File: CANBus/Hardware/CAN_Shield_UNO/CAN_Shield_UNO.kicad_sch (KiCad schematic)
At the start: 12 parts, among them J1 Power, J2 Digital/PWM, J3 Analog, J4 Digital/PWM, J7 Screw_Terminal_01x02, U2 TCAN1051HGV

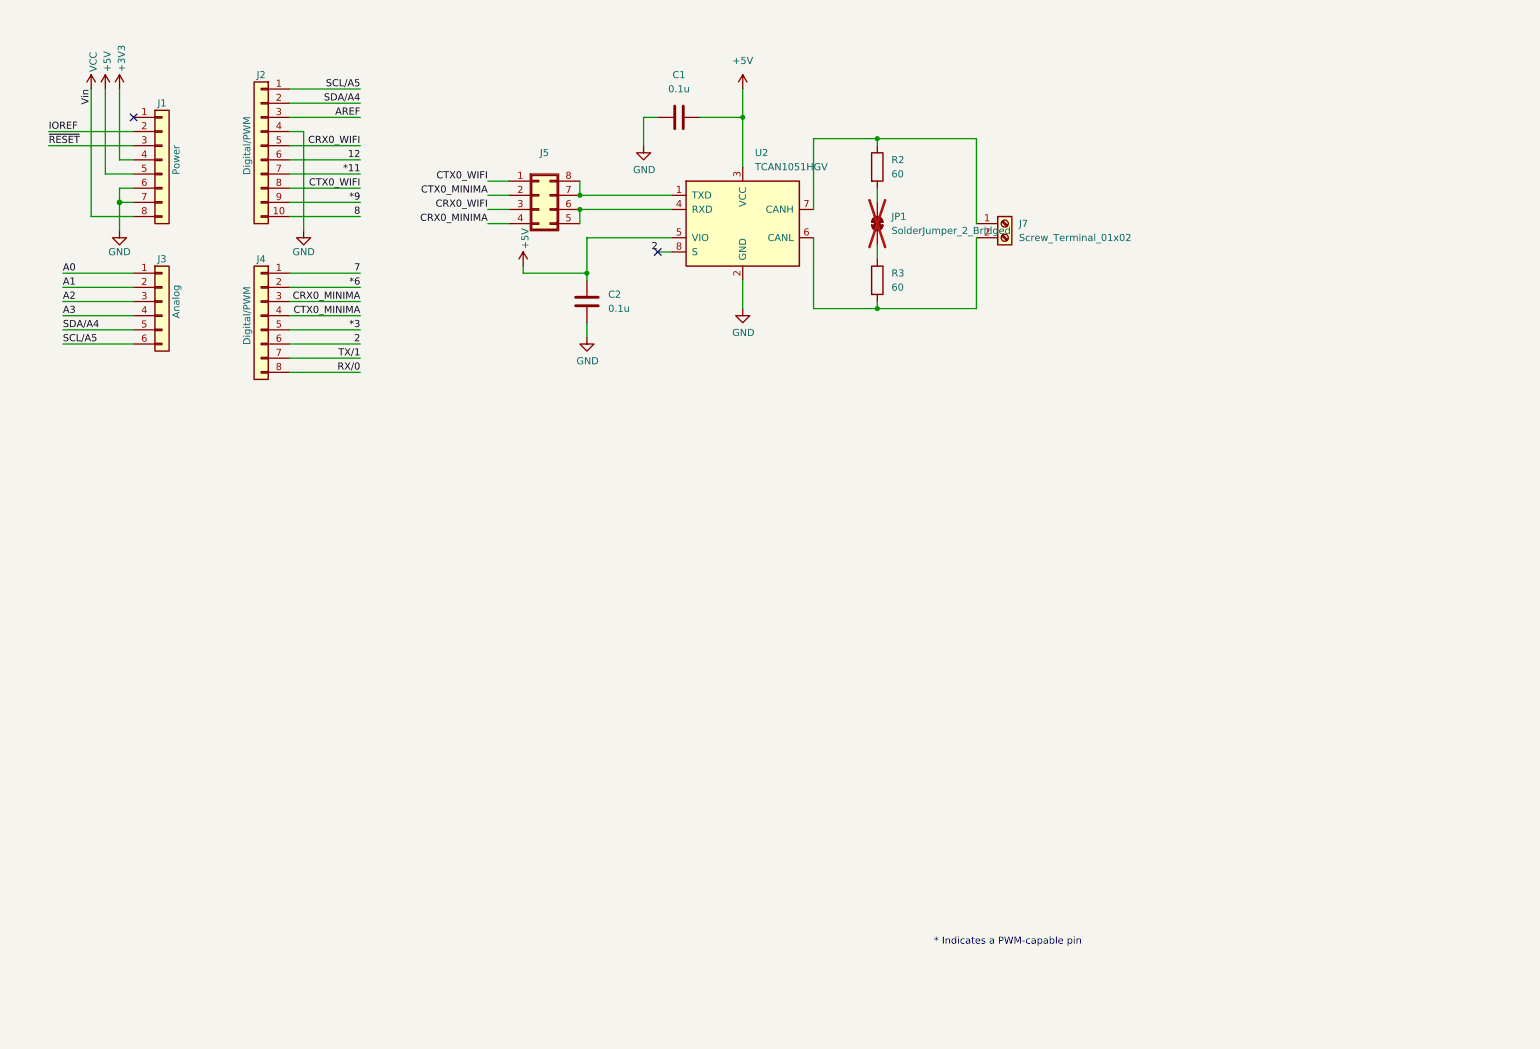
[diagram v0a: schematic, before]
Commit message: feat(hw): to add hardware components
- Replacing the CAN Bus driver
- Adding a pull-down resistor to the CS pin
- Adding a 1nF capacitor to the 120 ohm terminating resistor
- Adding 2EDN7534F (54 Gate driver) channels to handle high current outputs; in addition adding a diode to power them if the board is only powered through USB
- Adding TL4050A50IDBZT (Precision micropower shunt voltage) to generate a precise 5V reference
- Adding protection diodes for A0 and A1 analog inputs
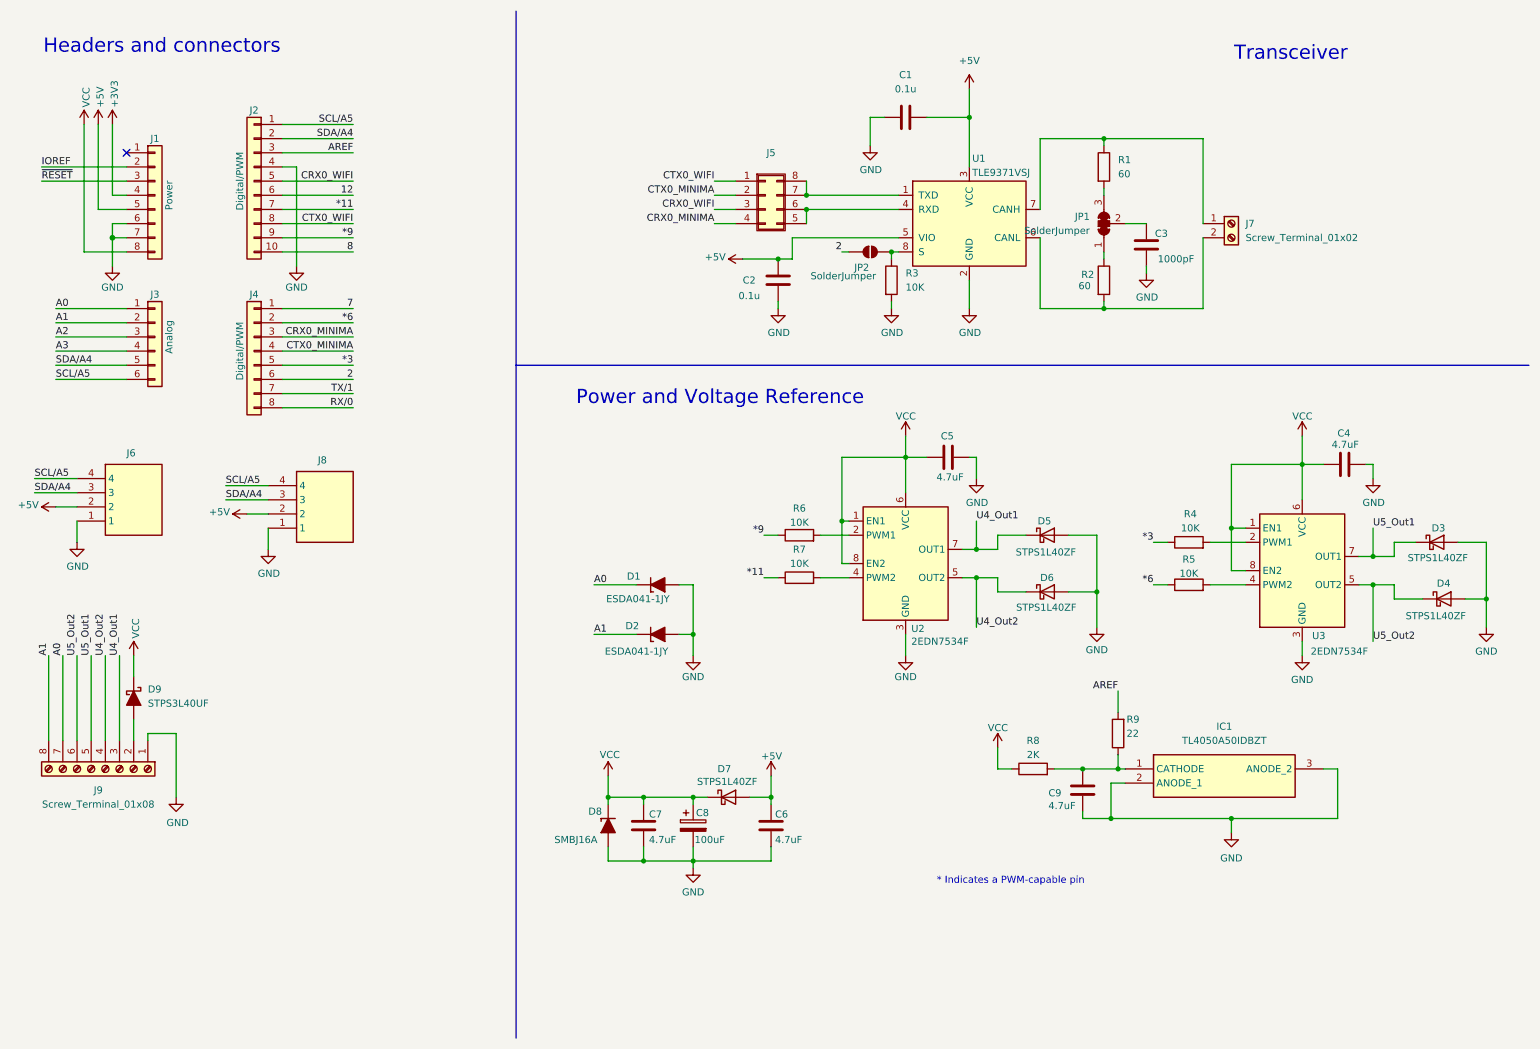
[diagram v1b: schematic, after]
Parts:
- removed JP1: SolderJumper_2_Bridged, Jumper:SolderJumper-2_P1.3mm_Bridged_Pad1.0x1.5mm, symbol Jumper:SolderJumper_2_Bridged
- added C3: 1000pF, Capacitor_SMD:C_0805_2012Metric_Pad1.18x1.45mm_HandSolder, symbol Device:C
- added C4, C5, C6, C7, C9: 4.7uF, Capacitor_SMD:C_1210_3225Metric_Pad1.33x2.70mm_HandSolder, symbol Device:C
- added C8: 100uF, Capacitor_SMD:CP_Elec_6.3x7.7, symbol PCM_Capacitor_AKL:CP_SMD_D6.3mm_H7.7mm
- added D1, D2: ESDA041-1JY, PCM_Diode_SMD_AKL:D_SOD-323, symbol PCM_Diode_TVS_AKL:SD05
- added D3, D4, D5, D6, D7: STPS1L40ZF, Diode_SMD:D_SOD-123, symbol Diode:MBR0540
- added D8: SMBJ16A, Diode_SMD:D_SMB, symbol PCM_Diode_TVS_AKL:SMBJ16A
- added D9: STPS3L40UF, Diode_SMD:D_SMB, symbol PCM_Diode_Schottky_AKL:STPS3L40UF
- added IC1: TL4050A50IDBZT, Package_TO_SOT_SMD:SOT-23-3, symbol TL4050A50IDBZT:TL4050A50IDBZT
- added J6, J8: Grove connector, Connector_PinHeader_2.54mm:PinHeader_1x04_P2.54mm_Vertical, symbol 110990030:110990030
- added J9: Screw_Terminal_01x08, TerminalBlock:TerminalBlock_bornier-8_P5.08mm, symbol Connector:Screw_Terminal_01x08
- added JP1: SolderJumper, Jumper:SolderJumper-3_P1.3mm_Open_RoundedPad1.0x1.5mm_NumberLabels, symbol Jumper:SolderJumper_3_Bridged123
- added JP2: SolderJumper, Jumper:SolderJumper-2_P1.3mm_Open_RoundedPad1.0x1.5mm, symbol Jumper:SolderJumper_2_Open
- added R3, R4, R5, R6, R7: 10K, Resistor_SMD:R_1206_3216Metric_Pad1.30x1.75mm_HandSolder, symbol Device:R
- added R8: 2K, Resistor_SMD:R_1206_3216Metric_Pad1.30x1.75mm_HandSolder, symbol Device:R
- added R9: 22, Resistor_SMD:R_1206_3216Metric_Pad1.30x1.75mm_HandSolder, symbol Device:R
- added U2, U3: 2EDN7534F, Package_SO:Infineon_PG-DSO-8-27_3.9x4.9mm_EP2.65x3mm, symbol Driver_FET:PM8834
- C1, C2: LCSC# C38141 -> (none); Proveedor LCSC -> MOUSER; manf# 0805B104K500NT -> 767-0805B104K500NT
- J1, J2, J3, J4: Proveedor MOUSER/DIGIKEY -> MOUSER
- J5: manf# PZ254-2-04-Z-2.5-G1 -> PZ254-2-04-Z-2.5-G1
- J7: Proveedor STEREN -> MOUSER; manf# TRT-02 -> 651-1729128
- R1: renamed from R2; manf# 71-CRCW120660R0KNAIF -> KTR18EZPF62R0
- R2: renamed from R3; manf# 71-CRCW120660R0KNAIF -> KTR18EZPF62R0
- U1: renamed from U2; value TCAN1051HGV -> TLE9371VSJ; footprint Package_SO:SOIC-8_3.9x4.9mm_P1.27mm -> Package_SO:Infineon_PG-DSO-8-27_3.9x4.9mm_EP2.65x3mm; manf# 595-TCAN1051HGVDR -> 726-TLE9371VSJXTMA1
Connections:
- net *11: now also R7.1
- net *3: now also R4.1
- net *6: now also R5.1
- net *9: now also R6.1
- net +5V: now also C6.2, D7.2 (A), J6.2, J8.2
- net 2: now also JP2.1 (A); no longer U1.8 (S)
- net A0: now also D1.1 (K), J9.7 (Pin_7)
- net A1: now also D2.1 (K), J9.8 (Pin_8)
- net AREF: now also R9.2
- net GND: now also C3.2, C4.2, C5.2, C6.1, C7.1, C8.2, C9.1, D1.2 (A), D2.2 (A), D3.2 (A), D4.2 (A), D5.2 (A), D6.2 (A), D8.2 (A), IC1.2 (ANODE_1), IC1.3 (ANODE_2), J6.1, J8.1, J9.1 (Pin_1), R3.2, U2.3 (GND), U3.3 (GND)
- net SCL/A5: now also J6.4, J8.4
- net SDA/A4: now also J6.3, J8.3
- net VCC: now also C4.1, C5.1, C7.2, C8.1, D7.1 (K), D8.1 (K), D9.1 (K), R8.1, U2.1 (EN1), U2.6 (VCC), U2.8 (EN2), U3.1 (EN1), U3.6 (VCC), U3.8 (EN2)
- net at R2.1: now also JP1.1 (A)
- net at R1.2: now also JP1.3 (B)
- new net: C9.2, IC1.1 (CATHODE), R8.2, R9.1
- new net: R4.2, U3.2 (PWM1)
- new net: R7.2, U2.4 (PWM2)
- new net: D9.2 (A), J9.2 (Pin_2)
- new net: R5.2, U3.4 (PWM2)
- new net: JP2.2 (B), R3.1, U1.8 (S)
- new net: C3.1, JP1.2 (C)
- new net: R6.2, U2.2 (PWM1)
- new net U4_Out1: D5.1 (K), J9.3 (Pin_3), U2.7 (OUT1)
- new net U4_Out2: D6.1 (K), J9.4 (Pin_4), U2.5 (OUT2)
- new net U5_Out1: D3.1 (K), J9.5 (Pin_5), U3.7 (OUT1)
- new net U5_Out2: D4.1 (K), J9.6 (Pin_6), U3.5 (OUT2)
- no-connect marks 2 -> 1
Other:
- note added: "Headers and connectors"
- note added: "Power and Voltage Reference"
- note added: "Transceiver"
- company: (none) -> Electronic Cats in collaboration with Imre
- title: (none) -> CAN Bus Shield for Arduino UNO
- moved on the sheet: C1, C2, J1, J2, J3, J4, J5, J7, R1, R2, U1
